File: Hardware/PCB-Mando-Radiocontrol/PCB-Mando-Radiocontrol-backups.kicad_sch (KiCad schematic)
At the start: 11 parts, among them J1 Arduino_Nano_Header, J2 HEADER_2, SW1 SW_SPDT, U1 Nrf24l01, U2 AMS1117-5.0

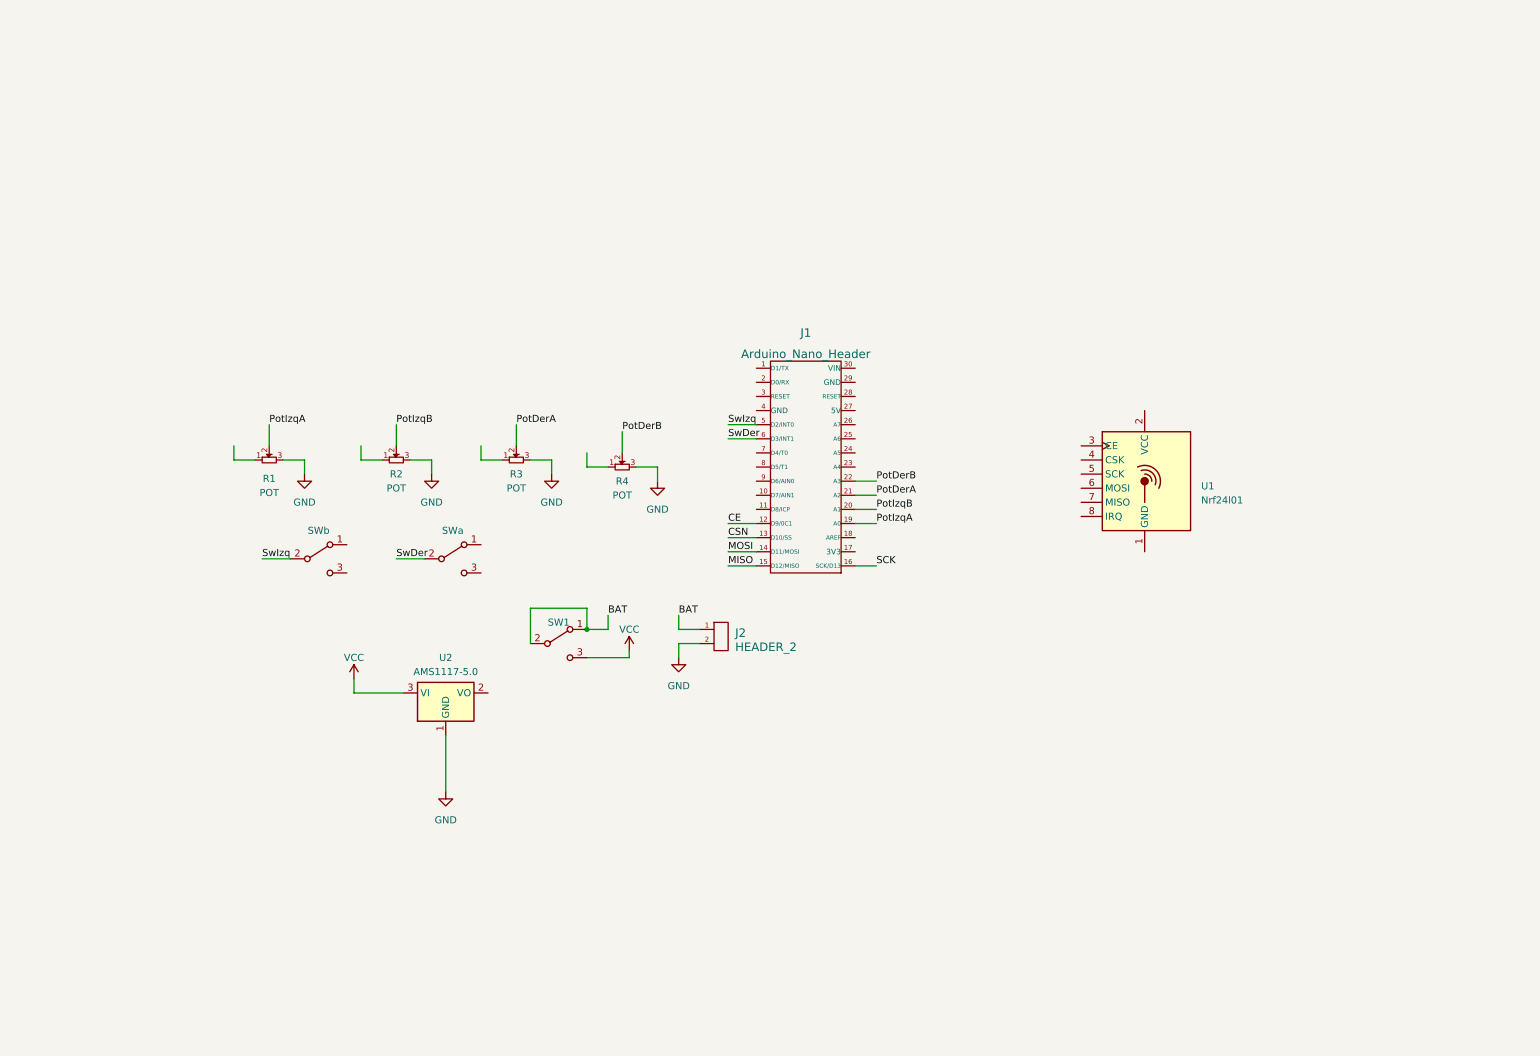
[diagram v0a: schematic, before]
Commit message: esquematico del pcb del radiocontrol terminado, falta acomoda los componentes y empezar el pcb
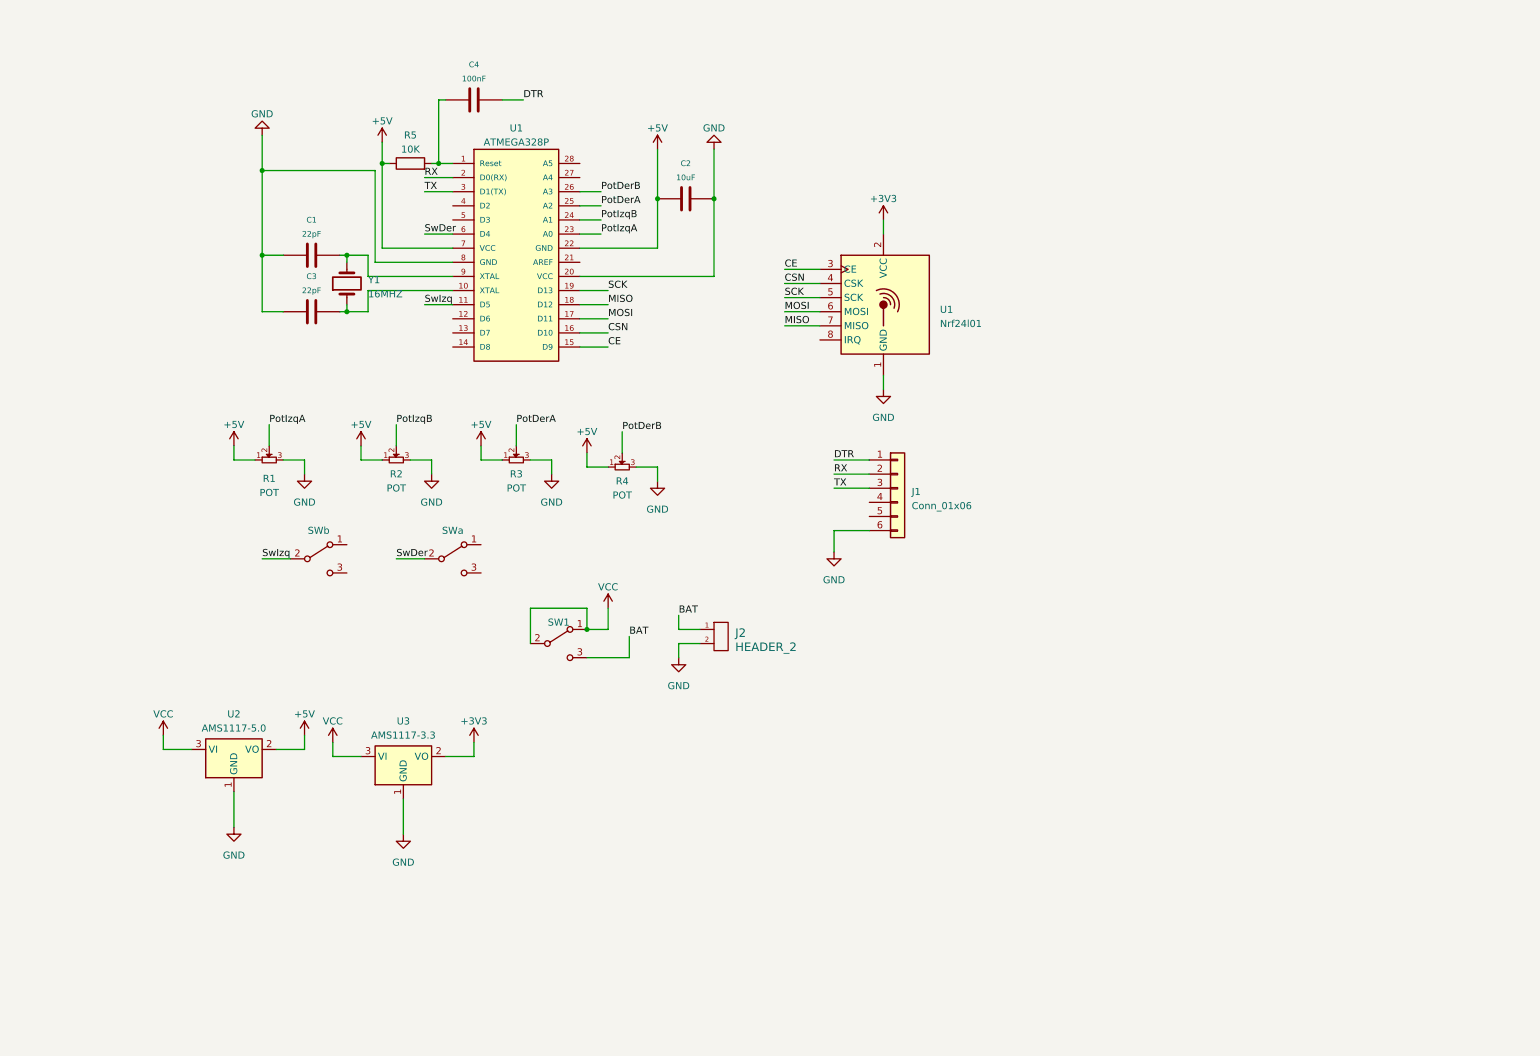
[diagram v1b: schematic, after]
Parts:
- removed J1: Arduino_Nano_Header, symbol EESTN5:Arduino_Nano_Header
- added C1, C3: 22pF, symbol EESTN5:C
- added C2: 10uF, symbol EESTN5:C
- added C4: 100nF, symbol EESTN5:C
- added J1: Conn_01x06, symbol EESTN5:Conn_01x06
- added R5: 10K, symbol Device:R
- added U1: ATMEGA328P, symbol EESTN5:ATMEGA328P-PU
- added U3: AMS1117-3.3, Package_TO_SOT_SMD:SOT-223-3_TabPin2, symbol Regulator_Linear:AMS1117-3.3
- added Y1: 16MHZ, symbol Device:Crystal
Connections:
- net BAT: now also SW1.3 (C); no longer SW1.1 (A), SW1.2 (B)
- net CE: now also U1.3 (CE), U1.15 (D9)
- net CSN: now also U1.4 (CSK), U1.16 (D10)
- net GND: now also U1.1 (GND), C1.1, C2.2, C3.1, J1.6 (Pin_6), U1.20 (VCC), U1.8 (GND), U3.1 (GND)
- net MISO: now also U1.7 (MISO), U1.18 (D12)
- net MOSI: now also U1.6 (MOSI), U1.17 (D11)
- net PotDerA: now also U1.25 (A2)
- net PotDerB: now also U1.26 (A3)
- net PotIzqA: now also U1.23 (A0)
- net PotIzqB: now also U1.24 (A1)
- net SCK: now also U1.5 (SCK), U1.19 (D13)
- net SwDer: now also U1.6 (D4)
- net SwIzq: now also U1.11 (D5)
- net VCC: now also SW1.1 (A), SW1.2 (B), U3.3 (VI); no longer SW1.3 (C)
- net +5V: now reaches R2.1
- net +5V: now also R1.1, R3.1, R4.1, U2.2 (VO), C2.1, R5.1, U1.22 (GND), U1.7 (VCC)
- net +3V3: now reaches U1.2 (VCC)
- net +3V3: now also U3.2 (VO)
- new net: C3.2, U1.10 (XTAL), Y1.1
- new net: C1.2, U1.9 (XTAL), Y1.2
- new net: C4.1, R5.2, U1.1 (Reset)
- new net DTR: C4.2, J1.1 (Pin_1)
- new net RX: J1.2 (Pin_2), U1.2 (D0(RX))
- new net TX: J1.3 (Pin_3), U1.3 (D1(TX))
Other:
- moved on the sheet: U1, U2

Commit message: esquematico terminado y ordenado
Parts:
- removed U2: AMS1117-5.0, Package_TO_SOT_SMD:SOT-223-3_TabPin2, symbol Regulator_Linear:AMS1117-5.0
- added C10, C12, C6, C7: 0.1uF, symbol EESTN5:C
- added C11, C5: 10uF, symbol EESTN5:C
- added C8, C9: 1uF, symbol EESTN5:C
- added U4: AMS1117-5.0, Package_TO_SOT_SMD:SOT-223-3_TabPin2, symbol Regulator_Linear:AMS1117-5.0
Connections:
- net +3V3: now also C5.1, C6.1
- net +5V: now also C11.1, C12.1, U4.2 (VO)
- net GND: now also C10.2, C11.2, C12.2, C5.2, C6.2, C7.2, C8.2, C9.2, U4.1 (GND)
- net VCC: now also C10.1, C7.1, C8.1, C9.1, U4.3 (VI)
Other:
- note added: "Alimentación"
- note added: "Interruptores"
- note added: "MCU"
- note added: "Modulo Nrf24l01"
- note added: "Programador"
- note added: "Sticks"
- moved on the sheet: C1, C2, C3, C4, J1, J2, R1, R2, R3, R4, R5, SW1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

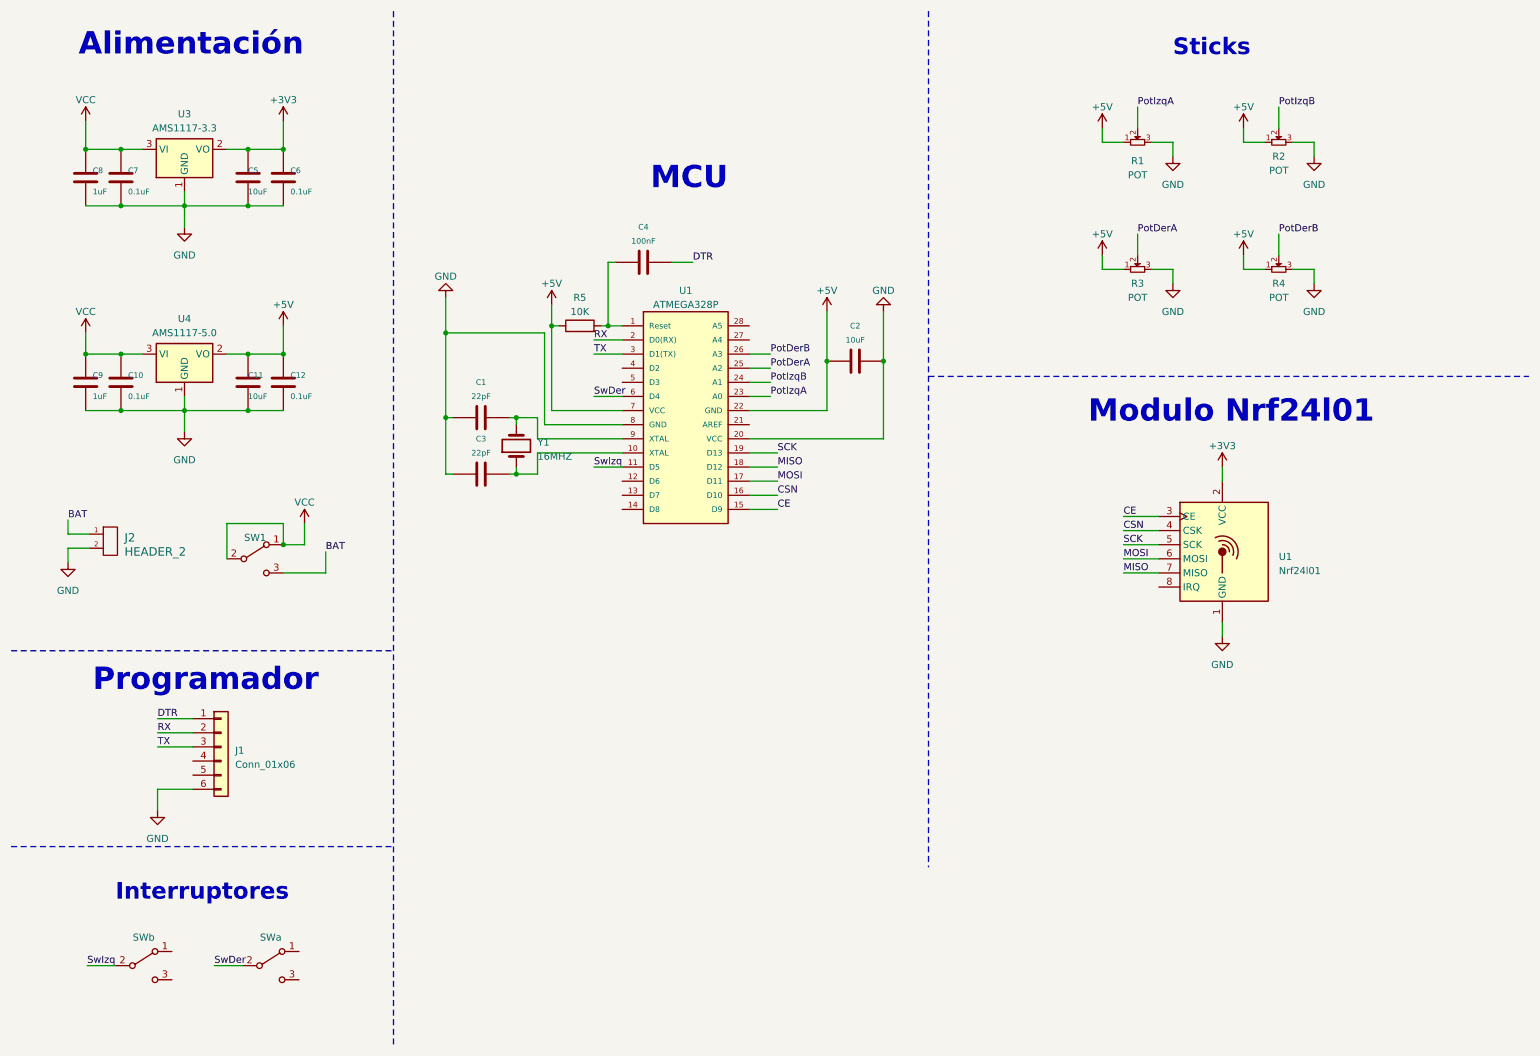
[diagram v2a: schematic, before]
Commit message: arregle errores de orden y los capacitores queda resolver conexiones si son las correctas , en programador y mcu
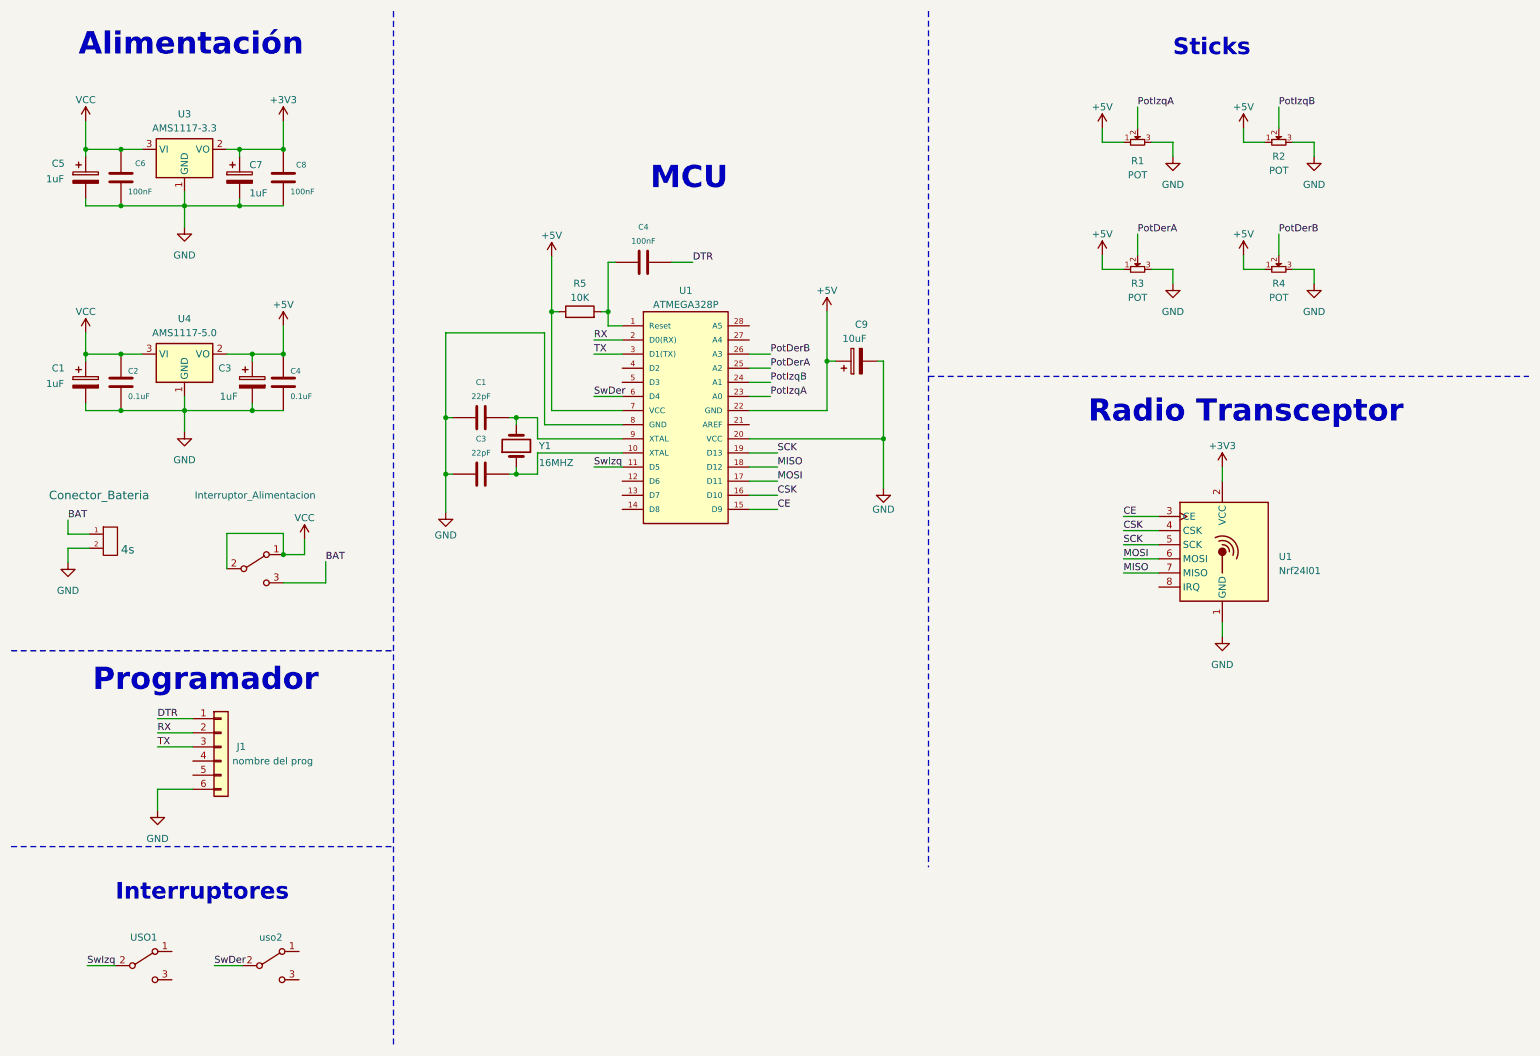
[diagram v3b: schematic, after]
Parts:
- removed C11, C2, C5: 10uF, symbol EESTN5:C
- removed C8, C9: 1uF, symbol EESTN5:C
- added C1, C3, C5, C7: 1uF, symbol Device:C_Polarized
- added C9: 10uF, symbol Device:C_Polarized
- C6: renamed from C7; value 0.1uF -> 100nF
- C8: renamed from C6; value 0.1uF -> 100nF
- Conector_Bateria: renamed from J2; value HEADER_2 -> 4s
- J1: value Conn_01x06 -> nombre del prog
- renumbered C10 to C2, C12 to C4, SW1 to Interruptor_Alimentacion, SWb to USO1, SWa to uso2
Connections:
- net +3V3: now also C7.1
- net +5V: now also C3.1, C9.1
- net GND: now also C1.2, C3.2, C5.2, C7.2, C9.2
- net VCC: now also C1.1, C5.1
- net CSN renamed CSK
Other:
- note added: "Radio Transceptor"
- note removed: "Modulo Nrf24l01"
- moved on the sheet: Interruptor_Alimentacion, R5

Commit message: huellas asignadas correctamente
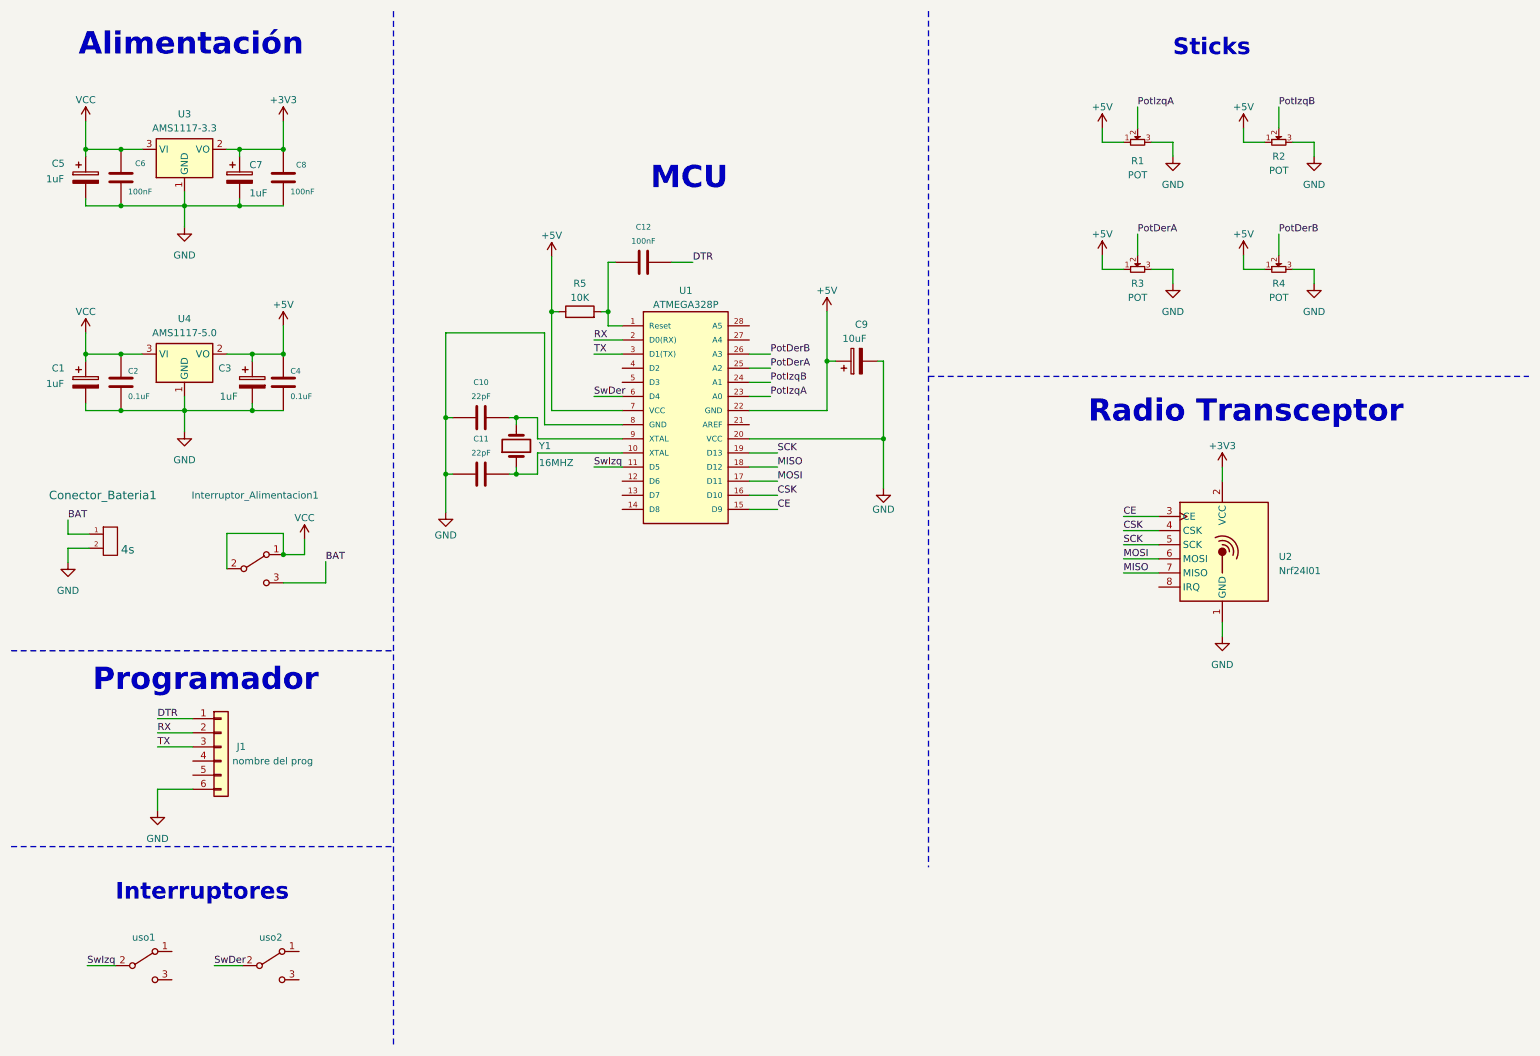
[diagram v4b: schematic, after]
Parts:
- C1, C3, C5, C7, C9: footprint (none) -> EESTN5:CAP_ELEC_5x11mm
- C10: renamed from C1; footprint (none) -> EESTN5:CAP_ELEC_5x11mm
- C11: renamed from C3; footprint (none) -> EESTN5:CAP_ELEC_5x11mm
- C12: renamed from C4; footprint (none) -> EESTN5:CAP_0.1
- C2, C4, C6, C8: footprint (none) -> EESTN5:CAP_0.1
- Conector_Bateria1: renamed from Conector_Bateria; footprint (none) -> EESTN5:Pin_Header_2
- Interruptor_Alimentacion1: renamed from Interruptor_Alimentacion; footprint (none) -> EESTN5:Pin_Header_3
- J1: footprint (none) -> EESTN5:Pin_Header_6
- R1, R2, R3, R4: footprint (none) -> PotStick:XDCR_COM-09032
- R5: footprint (none) -> EESTN5:RES0.3
- U1: footprint (none) -> EESTN5:DIP_28-300_socket
- U2: renamed from U1; footprint (none) -> RF_Module:nRF24L01_Breakout
- Y1: footprint (none) -> Cristal:XTAL_XT9S20ANA16M
- uso1: renamed from USO1; footprint (none) -> EESTN5:Pin_Header_3
- uso2: footprint (none) -> EESTN5:Pin_Header_3

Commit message: SCH terminado y PCB a continuar
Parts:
- removed R1, R2, R3, R4: POT, PotStick:XDCR_COM-09032, symbol EESTN5:POT
- added U5, U6: COM-09032, PotStick:XDCR_COM-09032, symbol COM-09032:COM-09032
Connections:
- net +5V: now also U5.H1 (H+), U5.V1 (V+), U6.H1 (H+), U6.V1 (V+)
- net GND: now also U5.H3 (H-), U5.S1 (SHIELD), U5.S2 (SHIELD), U5.S3 (SHIELD), U5.S4 (SHIELD), U5.V3 (V-), U6.H3 (H-), U6.S1 (SHIELD), U6.S2 (SHIELD), U6.S3 (SHIELD), U6.S4 (SHIELD), U6.V3 (V-)
- net PotDerA: now also U5.H2 (H)
- net PotDerB: now also U5.V2 (V)
- net PotIzqA: now also U6.H2 (H)
- net PotIzqB: now also U6.V2 (V)
